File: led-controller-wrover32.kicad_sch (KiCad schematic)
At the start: 52 parts, among them J101 Micro USB, J102 UART, J103 STATUS OUT, J104 USB_B_Micro, J105 POWER IN, J106 Conn_01x02 DNF, J107 I2C, J108 5V_LOGIC, Q101 UMH3N, Q102 BSS138, Q103 EM6K7T2R, U102 USBUF02W6, U103 ESP32-S3-WROOM-2-N32R8V, U104 MAX3379EETD, U105 AP22815AWT-7

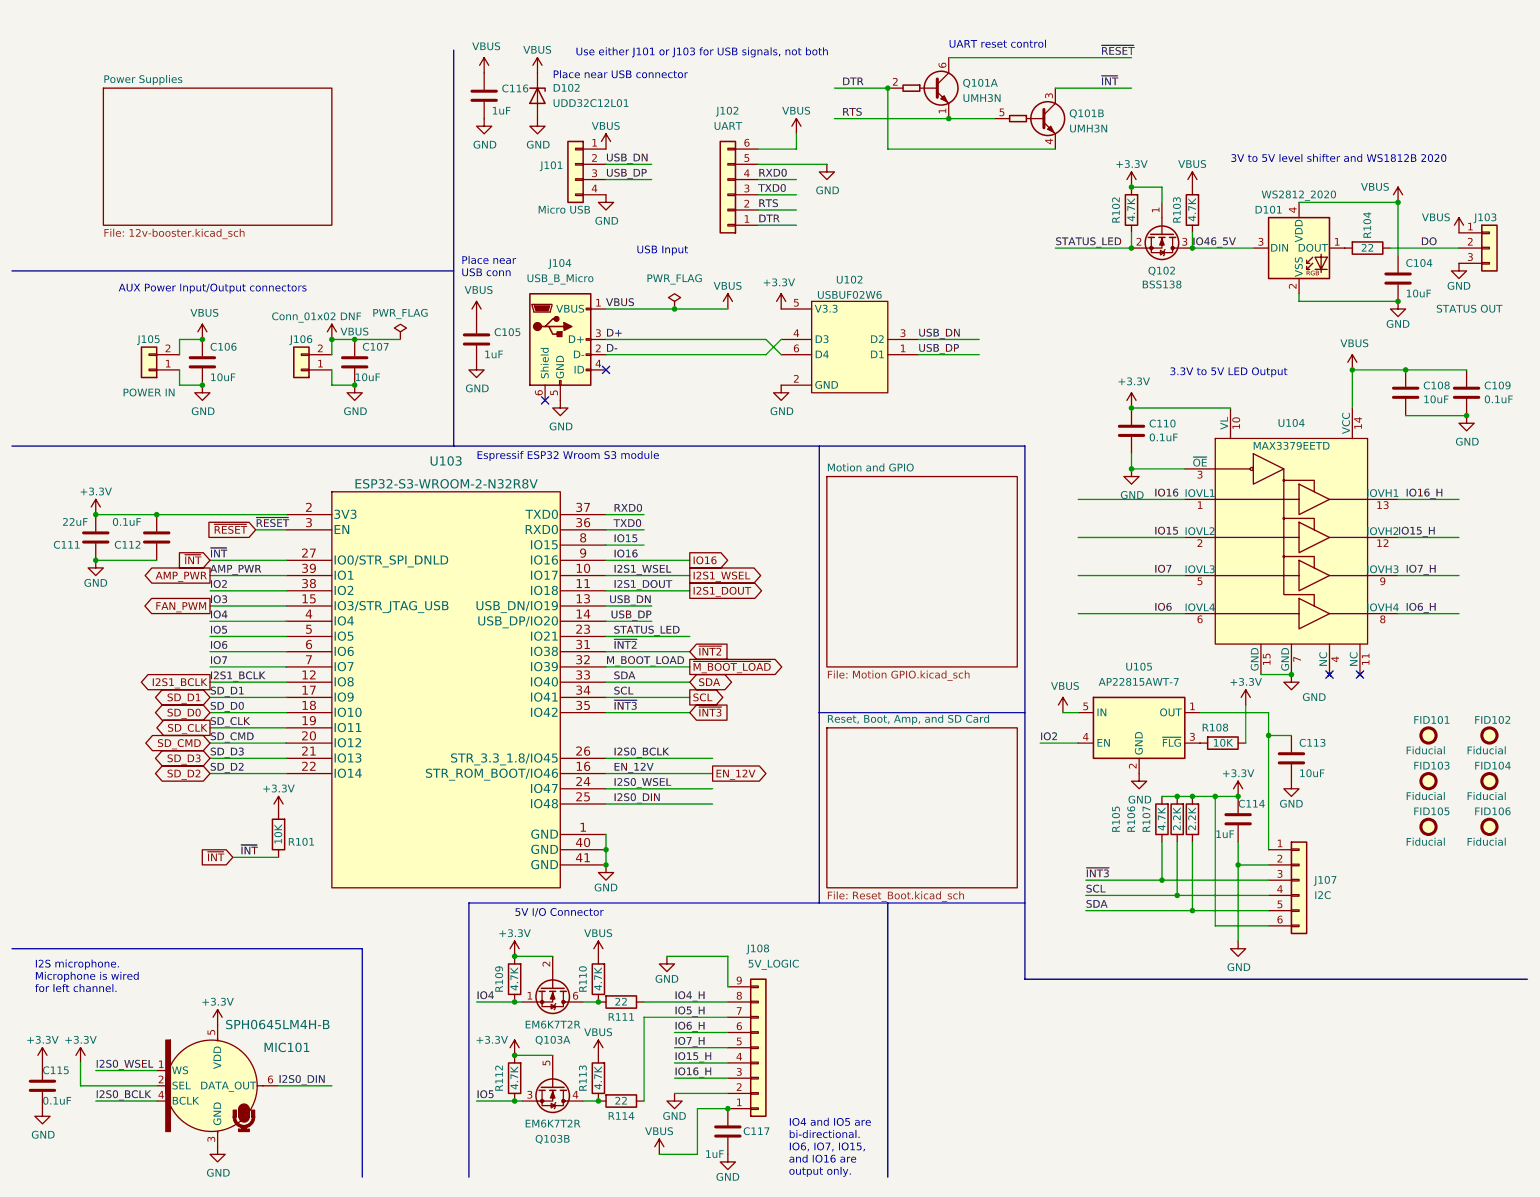
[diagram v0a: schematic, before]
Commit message: More updates
- Changed obsolete unidirectional level shifter to open-collector level shifter
- Replaced BSS138 level shifters with dedicated level shifter
- Changed all 5V I/O pins to have 33 ohm resistor in series
- Changed a few capacitors
- Cleanup tracks, vias, silkscreen, etc.

Signed-off-by: Aaron Williams <aaron.w2@gmail.com>
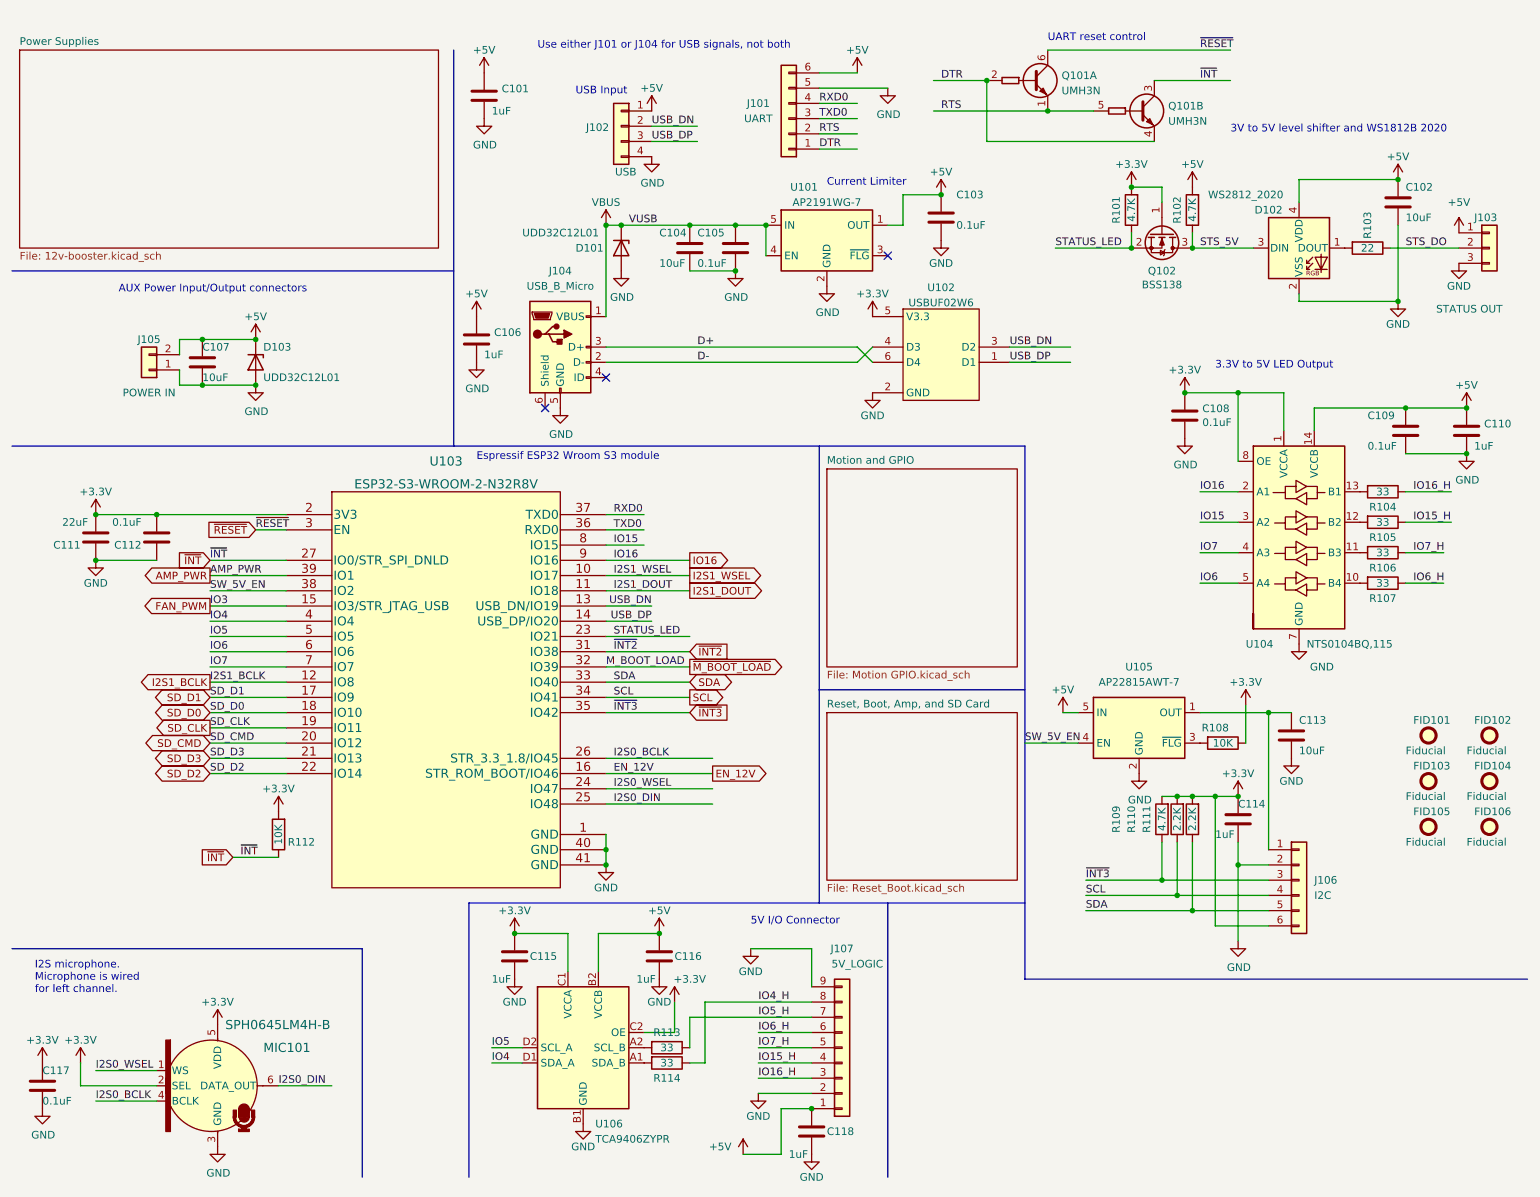
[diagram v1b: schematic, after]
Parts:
- removed C108: 10uF, Capacitor_SMD:C_0603_1608Metric, symbol Device:C
- removed J106: Conn_01x02 DNF, Connector_PinHeader_2.54mm:PinHeader_1x02_P2.54mm_Vertical, symbol Connector_Generic:Conn_01x02
- removed Q103: EM6K7T2R, Package_TO_SOT_SMD:SOT-563, symbol Transistor_FET:EM6K7T2R
- removed R109, R110, R112, R113: 4.7K, Resistor_SMD:R_0402_1005Metric, symbol Device:R
- removed U104: MAX3379EETD, Aaron:TDFN-14_3x3mm_P0.4mm_EP1.78x2.35mm, symbol Aaron:MAX3379EETD
- added C103, C105: 0.1uF, Capacitor_SMD:C_0402_1005Metric, symbol Device:C
- added C110, C115, C116: 1uF, Capacitor_SMD:C_0402_1005Metric, symbol Device:C
- added D103: UDD32C12L01, Diode_SMD:D_SOD-323, symbol Device:D_Zener
- added R104, R105, R106, R107: 33, Resistor_SMD:R_0402_1005Metric, symbol Device:R
- added U101: AP2191WG-7, Package_TO_SOT_SMD:SOT-23-5, symbol Power_Management:AP2191WG-7
- added U104: NTS0104BQ,115, Package_TO_SOT_SMD:SOT-762-1, symbol Logic_LevelTranslator:NTS0104BQ,115
- added U106: TCA9406ZYPR, Package_BGA:Texas_DSBGA-8_0.9x1.9mm_Layout2x4_P0.5mm, symbol Interface:TCA9406ZYPR
- C104: renamed from C107; now in the parts list
- J101: renamed from J102; MANUFACTURER (none) -> Molex; MFR (none) -> Molex
- J102: renamed from J101; value Micro USB -> USB
- Q102: footprint Package_TO_SOT_SMD:SOT-23 -> Package_TO_SOT_SMD:SOT-323_SC-70
- R113: renamed from R111; value 22 -> 33
- R114: value 22 -> 33
- renumbered C116 to C101, C104 to C102, C105 to C106, C106 to C107, C110 to C108, C115 to C117, C117 to C118, D102 to D101, D101 to D102, J107 to J106, J108 to J107, R102 to R101, R103 to R102, R104 to R103, R105 to R109, R106 to R110, R107 to R111, R101 to R112
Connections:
- net +3V3: now also C115.1, U104.1 (VCCA), U104.8 (OE), U106.C1 (VCCA), U106.C2 (OE)
- net GND: now also C103.2, C105.2, C110.2, C115.2, C116.2, D103.2 (A), U101.2 (GND), U104.15 (GND), U104.7 (GND), U106.B1 (GND)
- net IO15: now also U104.3 (A2)
- net IO15_H: now also R105.1
- net IO16: now also U104.2 (A1)
- net IO16_H: now also R104.1
- net IO4: now also U106.D1 (SDA_A)
- net IO4_H: now also R114.1; no longer R113.1
- net IO5: now also U106.D2 (SCL_A)
- net IO5_H: now also R113.1; no longer R114.1
- net IO6: now also U104.5 (A4)
- net IO6_H: now also R107.1
- net IO7: now also U104.4 (A3)
- net IO7_H: now also R106.1
- net VBUS: now also C105.1, U101.4 (EN), U101.5 (IN); no longer C101.1, C102.1, C106.1, C107.1, C109.1, C118.1, D102.4 (VDD), J101.6 (Pin_6), J102.1 (Pin_1), J103.1 (Pin_1), J105.2 (Pin_2), J107.1 (Pin_1), R102.2, U105.5 (IN)
- net at R114.2: now also U106.A1 (SDA_B)
- net at R113.2: now also U106.A2 (SCL_B)
- net DO renamed STS_DO
- net IO2 renamed SW_5V_EN
- net IO46_5V renamed STS_5V
- new net: R104.2, U104.13 (B1)
- new net: R107.2, U104.10 (B4)
- new net: R106.2, U104.11 (B3)
- new net: R105.2, U104.12 (B2)
- new net +5V: C101.1, C102.1, C103.1, C106.1, C107.1, C109.1, C110.1, C116.1, C118.1, D102.4 (VDD), D103.1 (K), J101.6 (Pin_6), J102.1 (Pin_1), J103.1 (Pin_1), J105.2 (Pin_2), J107.1 (Pin_1), R102.2, U101.1 (OUT), U104.14 (VCCB), U105.5 (IN), U106.B2 (VCCB)
- no-connect marks 4 -> 3
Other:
- note added: "Current Limiter"
- note added: "Use either J101 or J104 for USB signals, not both"
- note removed: "IO4 and IO5 are bi-directional. IO6, IO7, IO15, and IO16 are output only."
- note removed: "Place near USB conn"
- note removed: "Place near USB connector"
- note removed: "Use either J101 or J103 for USB signals, not both"
- moved on the sheet: C102, C104, C108, C109, C113, C118, D101, J101, J102, J104, J107, Q101A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

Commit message: Multiple updates
- Changed input current limiter to ferrite bead
- Added pull-up for BNO085 boot mode
- Minor layout changes

Signed-off-by: Aaron Williams <aaron.w2@gmail.com>
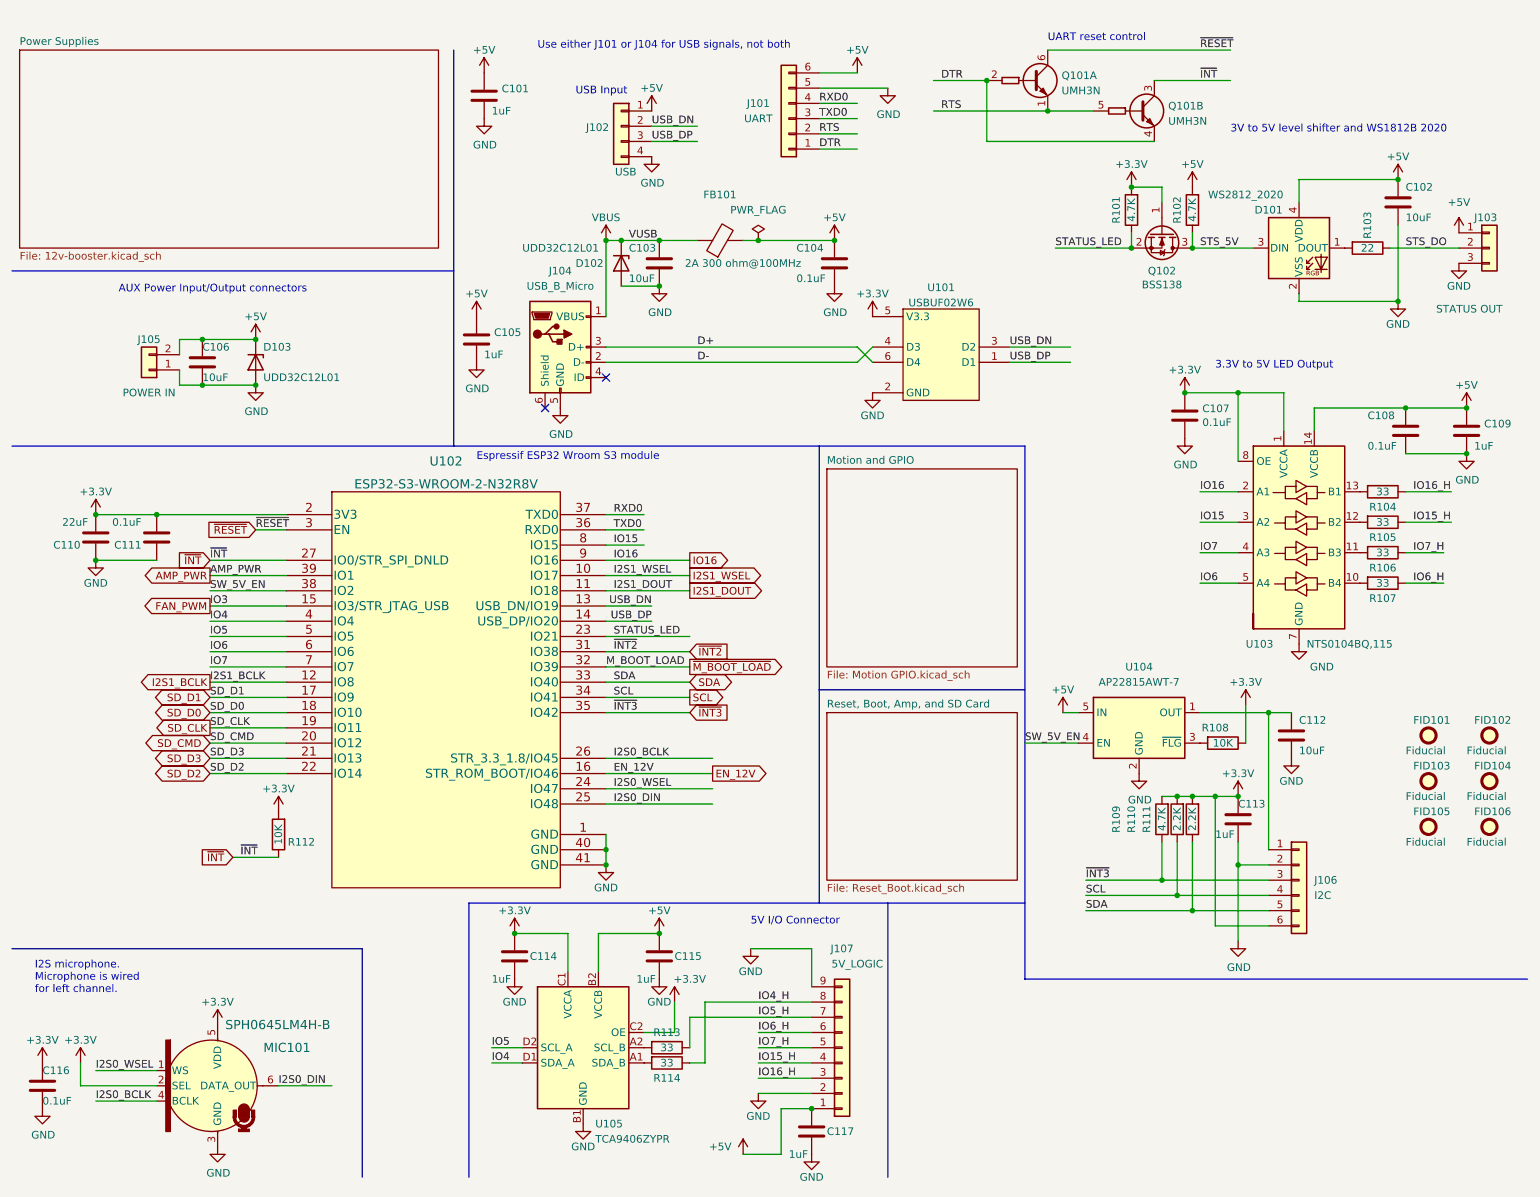
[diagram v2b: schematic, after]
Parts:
- removed C103: 0.1uF, Capacitor_SMD:C_0402_1005Metric, symbol Device:C
- removed U101: AP2191WG-7, Package_TO_SOT_SMD:SOT-23-5, symbol Power_Management:AP2191WG-7
- added FB101: 2A 300 ohm@100MHz, Inductor_SMD:L_0603_1608Metric, symbol Device:FerriteBead
- renumbered C104 to C103, C105 to C104, C106 to C105, C107 to C106, C108 to C107, C109 to C108, C110 to C109, C111 to C110, C112 to C111, C113 to C112, C114 to C113, C115 to C114, C116 to C115, C117 to C116, C118 to C117, D102 to D101, D101 to D102, U102 to U101, U103 to U102, U104 to U103, U105 to U104, U106 to U105
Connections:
- net +5V: now also C104.1, FB101.2
- net VBUS: now also FB101.1; no longer C104.1
- no-connect marks 3 -> 2
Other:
- note removed: "Current Limiter"
- moved on the sheet: C103, C104, D102

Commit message: More updates
- Removed 5V switch
- Added manual reset control of BNO085 to support booting remotely
- More minor cleanups
- Added jpeg renderings

Signed-off-by: Aaron Williams <aaron.w2@gmail.com>
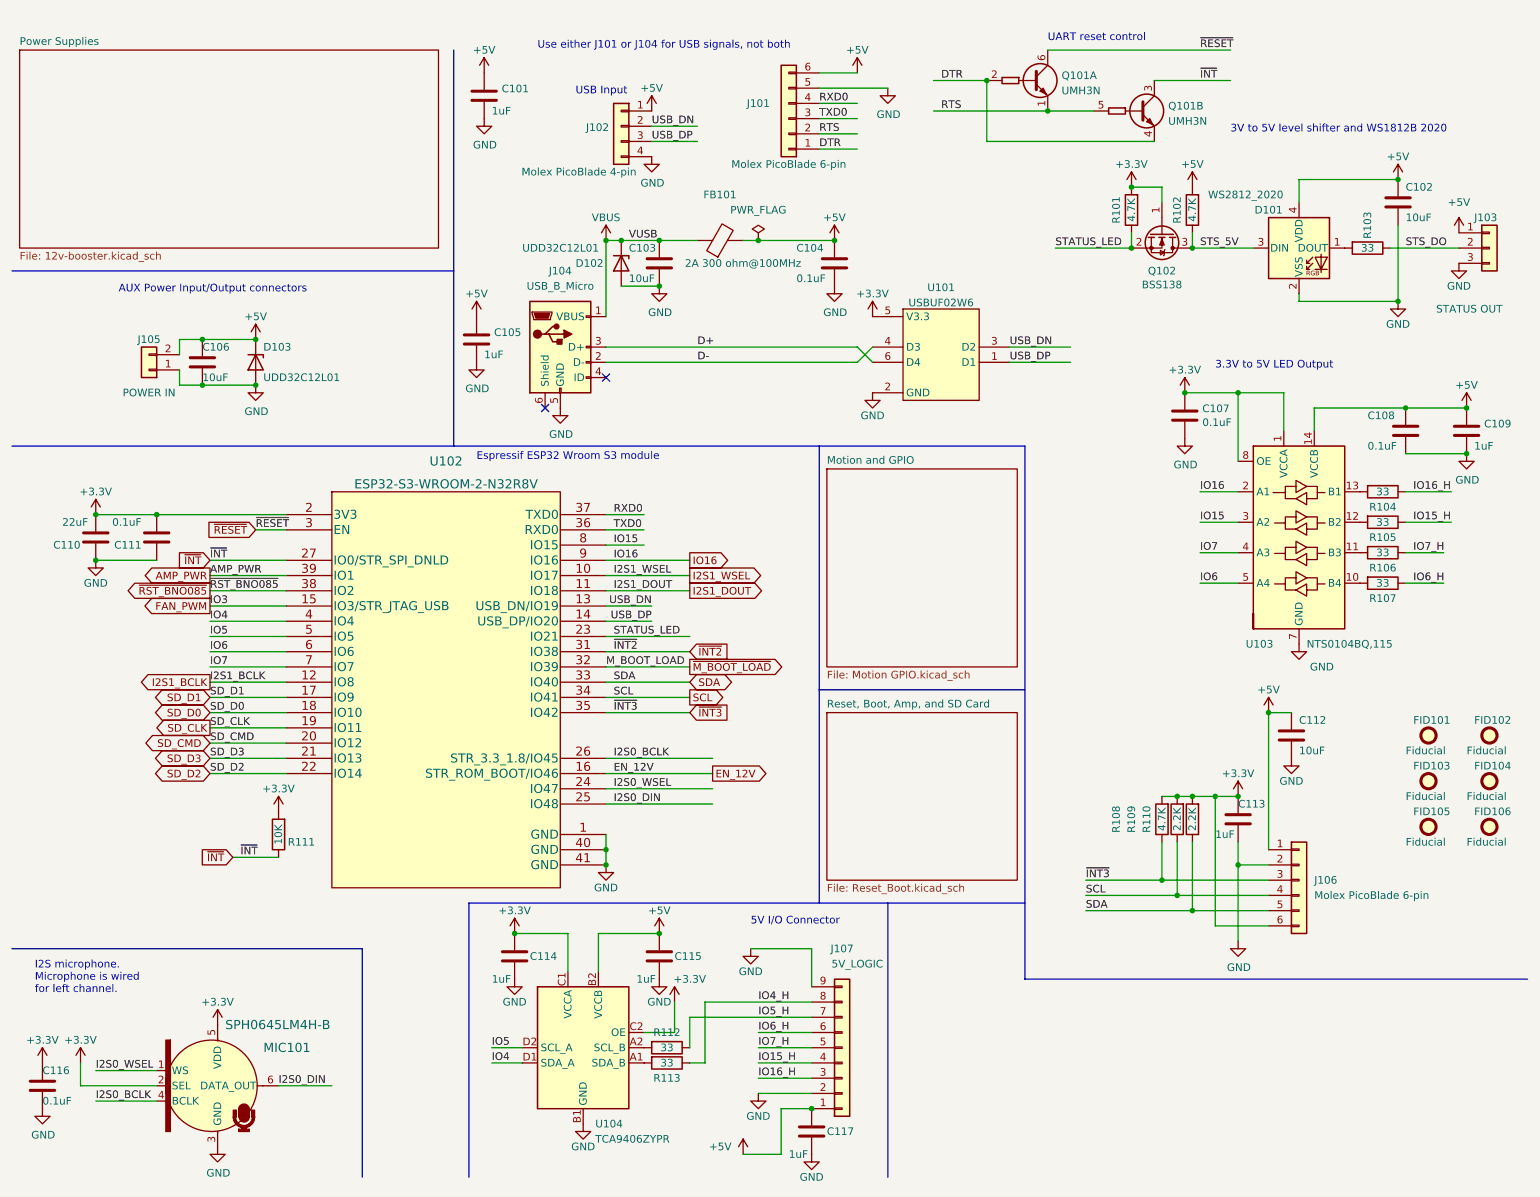
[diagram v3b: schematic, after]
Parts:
- removed R108: 10K, Resistor_SMD:R_0402_1005Metric, symbol Device:R
- removed U104: AP22815AWT-7, Package_TO_SOT_SMD:SOT-23-5, symbol Power_Management:AP22815AWT-7
- J101: value UART -> Molex PicoBlade 6-pin
- J102: value USB -> Molex PicoBlade 4-pin; DESC (none) -> Connector Header Through Hole 4 position 0.049" (1.25mm); MFR (none) -> Molex; MPN (none) -> 0530470410; SPN (none) -> WM1733-ND; SPURL (none) -> https://www.digikey.com/en/products/detail/molex/0530470410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
- J106: value I2C -> Molex PicoBlade 6-pin
- R103: value 22 -> 33
- U102: MFR (none) -> EspressIF
- renumbered R109 to R108, R110 to R109, R111 to R110, R112 to R111, R113 to R112, R114 to R113, U105 to U104
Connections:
- net +5V: now also C112.1, J106.1 (Pin_1)
- net SW_5V_EN renamed ~{RST_BNO085}
